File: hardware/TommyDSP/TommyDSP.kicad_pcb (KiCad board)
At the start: 2 copper layers, 35 parts, among them SW201 SW_Push, SW202 SW_Push, U201 W25Q128JVS, U202 DNF, U203 RP2350_60QFN, Y1 ABM8-272-T3

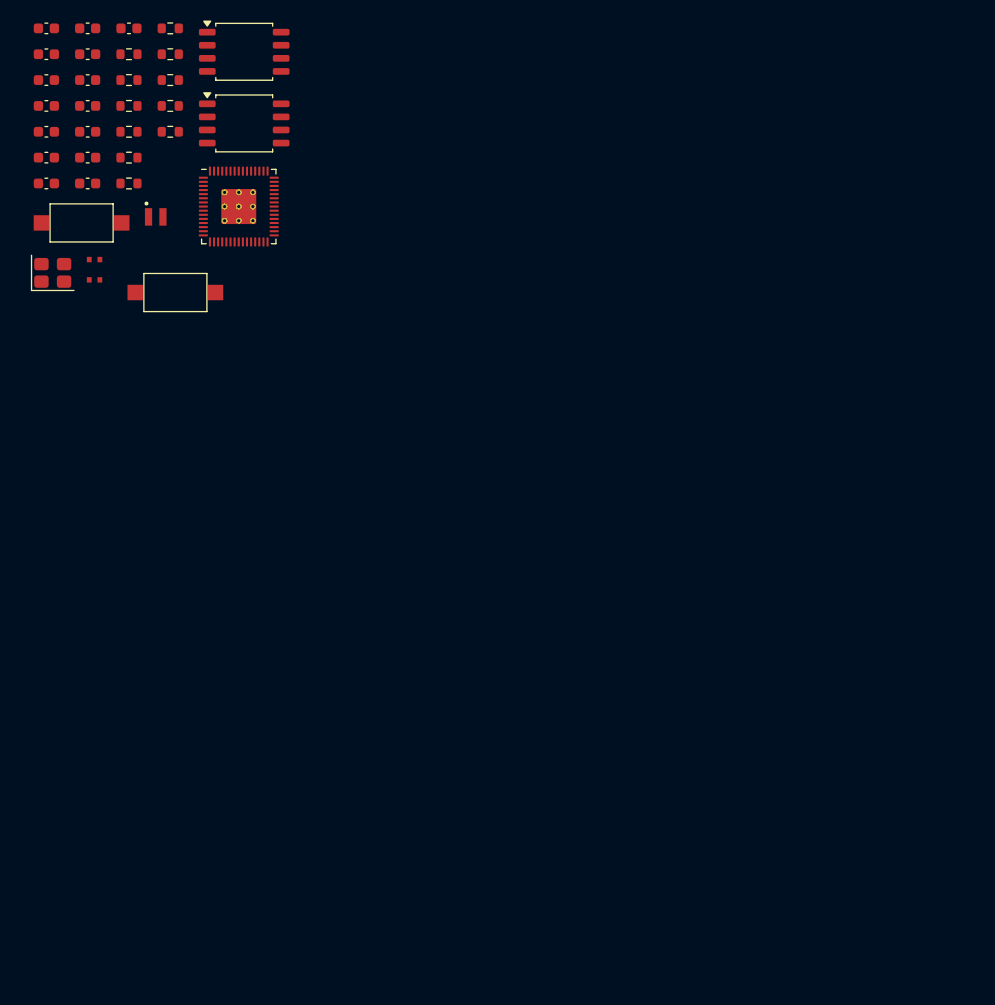
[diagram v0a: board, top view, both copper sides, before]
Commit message: hardware: finished PCB routing
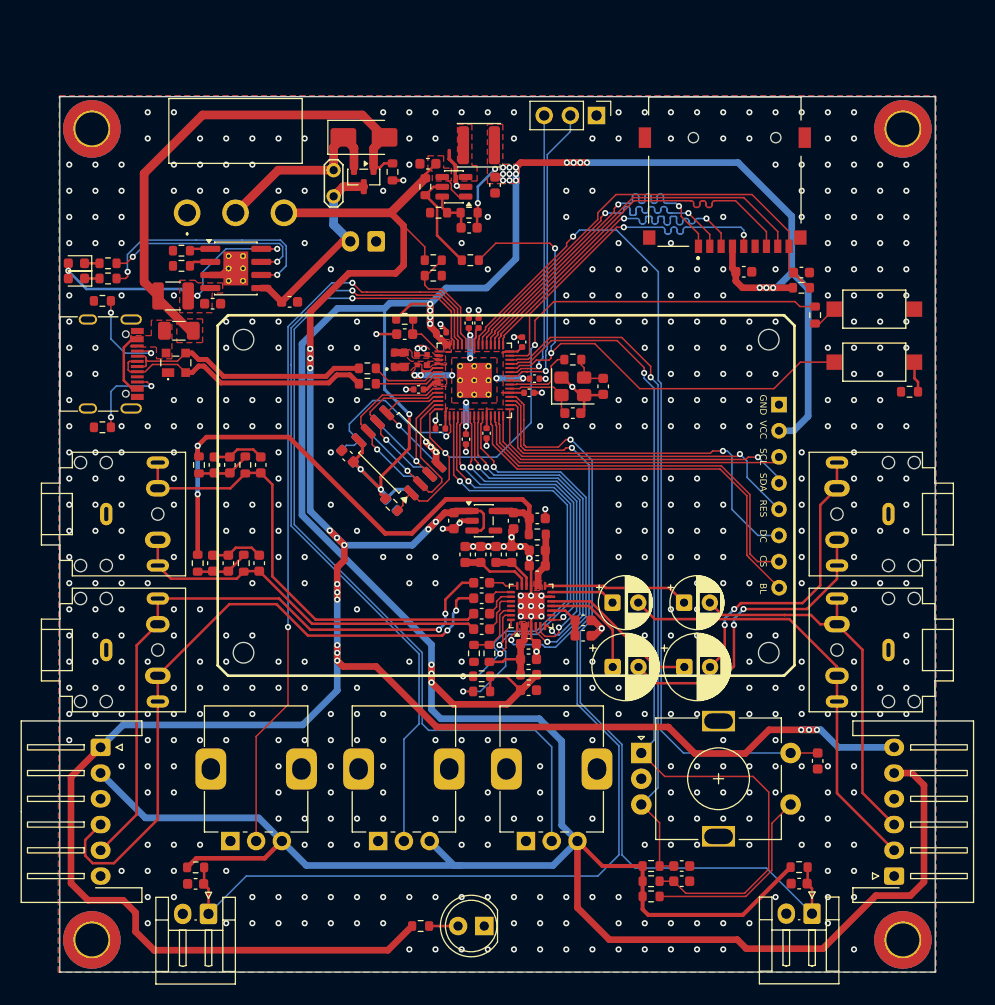
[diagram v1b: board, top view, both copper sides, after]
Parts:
- removed C3, C4: 15p, Capacitor_SMD:C_0603_1608Metric
- removed R2: 1k, Resistor_SMD:R_0603_1608Metric
- removed R209, R210: 27, Resistor_SMD:R_0603_1608Metric
- removed Y1: ABM8-272-T3, Crystal:Crystal_SMD_3225-4Pin_3.2x2.5mm
- added C216: 100n, Capacitor_SMD:C_0402_1005Metric, F.Cu at (158.1, 100.6)
- added C217: 100n, Capacitor_SMD:C_0402_1005Metric, F.Cu at (156.0, 96.8)
- added C301: 4.7u, Capacitor_SMD:C_0603_1608Metric, F.Cu at (171.9, 119.2)
- added C302: 4.7u, Capacitor_SMD:C_0603_1608Metric, F.Cu at (165.0, 112.8)
- added C303: 4.7u, Capacitor_SMD:C_0603_1608Metric, F.Cu at (162.0, 112.8)
- added C304: 100n, Capacitor_SMD:C_0603_1608Metric, F.Cu at (167.5, 109.3)
- added C305: 100n, Capacitor_SMD:C_0603_1608Metric, F.Cu at (171.9, 120.7)
- added C306: 100n, Capacitor_SMD:C_0603_1608Metric, F.Cu at (163.5, 112.8)
- added C307: 100n, Capacitor_SMD:C_0603_1608Metric, F.Cu at (160.5, 112.8)
- added C308: 4.7uF, Capacitor_SMD:C_0603_1608Metric, F.Cu at (166.7, 123.0)
- added C309: 4.7uF, Capacitor_SMD:C_0603_1608Metric, F.Cu at (167.5, 112.4)
- added C310: 100n, Capacitor_SMD:C_0603_1608Metric, F.Cu at (166.7, 121.5)
- added C311: 100n, Capacitor_SMD:C_0603_1608Metric, F.Cu at (167.5, 113.9)
- added C312: 100n, Capacitor_SMD:C_0603_1608Metric, F.Cu at (162.1, 120.1)
- added C313: 100n, Capacitor_SMD:C_0603_1608Metric, F.Cu at (162.1, 118.6)
- added C314: 1u, Capacitor_SMD:C_0603_1608Metric, F.Cu at (162.1, 117.1)
- added C315: 1u, Capacitor_SMD:C_0603_1608Metric, F.Cu at (162.1, 115.6)
- added C316: 220u, Capacitor_THT:CP_Radial_D6.3mm_P2.50mm, F.Cu at (181.8, 123.8)
- added C317: 220u, Capacitor_THT:CP_Radial_D6.3mm_P2.50mm, F.Cu at (174.8, 123.8)
- added C318: 4.7u, Capacitor_THT:CP_Radial_D5.0mm_P2.50mm, F.Cu at (181.8, 117.5)
- added C319: 4.7u, Capacitor_THT:CP_Radial_D5.0mm_P2.50mm, F.Cu at (174.8, 117.5)
- added C320: 10u, Capacitor_SMD:C_0603_1608Metric, F.Cu at (136.0, 113.7)
- added C321: 100n, Capacitor_SMD:C_0603_1608Metric, F.Cu at (137.5, 113.7)
- added C322: 10n, Capacitor_SMD:C_0603_1608Metric, F.Cu at (140.5, 113.7)
- added C323: 10u, Capacitor_SMD:C_0603_1608Metric, F.Cu at (136.2, 104.1)
- added C324: 100n, Capacitor_SMD:C_0603_1608Metric, F.Cu at (137.7, 104.1)
- added C325: 10n, Capacitor_SMD:C_0603_1608Metric, F.Cu at (140.7, 104.1)
- added C401: 4.7u, Capacitor_SMD:C_0603_1608Metric, F.Cu at (156.9, 74.9)
- added C402: 1u, Capacitor_SMD:C_0603_1608Metric, F.Cu at (159.4, 109.5)
- added C403: 10u, Capacitor_SMD:C_0603_1608Metric, F.Cu at (136.0, 88.5)
- added C404: 4.7u, Capacitor_SMD:C_0603_1608Metric, F.Cu at (165.2, 109.5)
- added C405: 120p, Capacitor_SMD:C_0603_1608Metric, F.Cu at (160.9, 81.1)
- added C406: 22u, Capacitor_SMD:C_0603_1608Metric, F.Cu at (163.4, 77.0)
- added C407: 10u, Capacitor_SMD:C_0603_1608Metric, F.Cu at (143.4, 88.3)
- added C501: 100n, Capacitor_SMD:C_0603_1608Metric, F.Cu at (134.3, 144.8)
- added C502: 100n, Capacitor_SMD:C_0603_1608Metric, F.Cu at (192.9, 144.8)
- added C503: 100n, Capacitor_SMD:C_0603_1608Metric, F.Cu at (187.6, 85.4)
- added C504: 100n, Capacitor_SMD:C_0603_1608Metric, F.Cu at (181.5, 144.6)
- added C505: 100n, Capacitor_SMD:C_0603_1608Metric, F.Cu at (181.5, 143.1)
- added C506: 100n, Capacitor_SMD:C_0603_1608Metric, F.Cu at (166.7, 126.0)
- added C507: 100n, Capacitor_SMD:C_0603_1608Metric, F.Cu at (193.2, 85.5)
- added C508: 100n, Capacitor_SMD:C_0603_1608Metric, F.Cu at (194.7, 132.9)
- added D401: LED GREEN, LED_SMD:LED_0603_1608Metric, F.Cu at (122.8, 86.0)
- added D402: LED RED, LED_SMD:LED_0603_1608Metric, F.Cu at (122.8, 84.5)
- added D403: SS34, Diode_SMD:D_SMA, F.Cu at (150.7, 72.3)
- added D404: PWR LED, LED_THT:LED_D5.0mm, F.Cu at (162.3, 148.9)
- added D501: CD143A-SR05, CD143A-SR05:CD143ASR05, F.Cu at (132.4, 94.2)
- added F501: 6V 1.1A, Fuse:Fuse_1206_3216Metric, F.Cu at (132.7, 91.1)
- added FB301: 120Ω@100MHz 2A 50mΩ@DC, Inductor_SMD:L_0603_1608Metric, F.Cu at (166.7, 124.5)
- added H101: M3 MountingHole, MountingHole:MountingHole_3.2mm_M3_DIN965_Pad_TopBottom, F.Cu at (124.2, 71.5)
- added H102: M3 MountingHole, MountingHole:MountingHole_3.2mm_M3_DIN965_Pad_TopBottom, F.Cu at (124.2, 150.2)
- added H103: M3 MountingHole, MountingHole:MountingHole_3.2mm_M3_DIN965_Pad_TopBottom, F.Cu at (203.0, 71.5)
- added H104: M3 MountingHole, MountingHole:MountingHole_3.2mm_M3_DIN965_Pad_TopBottom, F.Cu at (203.0, 150.2)
- added J401: Conn_01x02_Pin, Connector_JST:JST_XH_B2B-XH-A_1x02_P2.50mm_Vertical, B.Cu at (151.8, 82.4)
- added J501: USB_C_Receptacle_USB2.0_16P, Connector_USB:USB_C_Receptacle_G-Switch_GT-USB-7010ASV, F.Cu at (124.9, 94.3)
- added J502: PJ-307, Project:Jack_3.5mm_CUI_SJ1-3525N_Horizontal, F.Cu at (125.7, 108.9)
- added J503: XH-2.50mm Horizontal, Connector_JST:JST_EH_S2B-EH_1x02_P2.50mm_Horizontal, F.Cu at (135.6, 147.7)
- added J504: PJ-307, Project:Jack_3.5mm_CUI_SJ1-3525N_Horizontal, F.Cu at (125.7, 122.1)
- added J505: Conn_01x06_Pin, Connector_JST:JST_XH_S6B-XH-A-1_1x06_P2.50mm_Horizontal, F.Cu at (125.1, 131.6)
- added J506: PJ-307, Project:Jack_3.5mm_CUI_SJ1-3525N_Horizontal, F.Cu at (201.6, 108.9)
- added J507: XH-2.50mm Horizontal, Connector_JST:JST_EH_S2B-EH_1x02_P2.50mm_Horizontal, F.Cu at (194.2, 147.7)
- added J508: Conn_01x06_Pin, Connector_JST:JST_XH_S6B-XH-A-1_1x06_P2.50mm_Horizontal, F.Cu at (202.2, 144.1)
- added J509: Conn_01x03_Pin, Connector_PinHeader_2.54mm:PinHeader_1x03_P2.54mm_Vertical, F.Cu at (173.2, 70.2)
- added J510: PJ-307, Project:Jack_3.5mm_CUI_SJ1-3525N_Horizontal, F.Cu at (201.6, 122.1)
- added J511: Micro_SD_Card_Det1, TF-01A:TF01A, F.Cu at (185.7, 75.7)
- added JP401: Jumper_2_Open, TestPoint:TestPoint_2Pads_Pitch2.54mm_Drill0.8mm, F.Cu at (147.7, 78.0)
- added L401: 1u, Inductor_SMD:L_APV_ANR4020, F.Cu at (161.8, 73.1)
- added LCD501: 1.8'_ST7735_128x160_TFT_Module, ST7735-128x160-TFT-Module:1.8'_ST7735_128x160_TFT_Module, F.Cu at (167.8, 107.0)
- added Q401: AO3401A, Package_TO_SOT_SMD:SOT-23, F.Cu at (150.7, 76.2)
- added R101: 0, Resistor_SMD:R_0603_1608Metric, F.Cu at (161.0, 84.2)
- added R102: 4.7k, Resistor_SMD:R_0603_1608Metric, F.Cu at (162.1, 126.1)
- added R103: 4.7k, Resistor_SMD:R_0603_1608Metric, F.Cu at (162.1, 124.7)
- added R301: 0, Resistor_SMD:R_0603_1608Metric, F.Cu at (162.8, 122.4)
- added R302: 0, Resistor_SMD:R_0603_1608Metric, F.Cu at (161.3, 122.4)
- added R303: 10, Resistor_SMD:R_0603_1608Metric, F.Cu at (167.5, 110.9)
- added R304: 1k, Resistor_SMD:R_0603_1608Metric, F.Cu at (134.5, 113.7)
- added R305: 2.2k, Resistor_SMD:R_0603_1608Metric, F.Cu at (139.0, 113.7)
- added R306: 1k, Resistor_SMD:R_0603_1608Metric, F.Cu at (134.7, 104.1)
- added R307: 2.2k, Resistor_SMD:R_0603_1608Metric, F.Cu at (139.2, 104.1)
- added R401: 1k, Resistor_SMD:R_0603_1608Metric, F.Cu at (125.8, 86.0)
- added R402: 1k, Resistor_SMD:R_0603_1608Metric, F.Cu at (125.8, 84.5)
- added R403: 500k, Resistor_SMD:R_0603_1608Metric, F.Cu at (156.6, 77.1)
- added R404: 0.5, Resistor_SMD:R_1210_3225Metric, F.Cu at (132.1, 87.7)
- added R405: 225k, Resistor_SMD:R_0603_1608Metric, F.Cu at (160.9, 79.6)
- added R406: 50k, Resistor_SMD:R_0603_1608Metric, F.Cu at (157.9, 79.6)
- added R407: 1.2k, Resistor_SMD:R_0603_1608Metric, F.Cu at (132.9, 84.8)
- added R408: 0, Resistor_SMD:R_0603_1608Metric, F.Cu at (132.9, 83.3)
- added R409: 10k, Resistor_SMD:R_0603_1608Metric, F.Cu at (153.4, 75.7)
- added R410: 1k, Resistor_SMD:R_0603_1608Metric, F.Cu at (156.2, 148.9)
- added R501: 100k, Resistor_SMD:R_0603_1608Metric, F.Cu at (157.4, 84.2)
- added R502: 100k, Resistor_SMD:R_0603_1608Metric, F.Cu at (157.4, 85.8)
- added R503: 5.1k, Resistor_SMD:R_0603_1608Metric, F.Cu at (125.3, 88.2)
- added R504: 5.1k, Resistor_SMD:R_0603_1608Metric, F.Cu at (125.3, 100.5)
- added R505: 100k, Resistor_SMD:R_0603_1608Metric, F.Cu at (134.3, 143.2)
- added R506: 100k, Resistor_SMD:R_0603_1608Metric, F.Cu at (192.9, 143.2)
- added R507: 100k, Resistor_SMD:R_0603_1608Metric, F.Cu at (178.6, 144.6)
- added R508: 100k, Resistor_SMD:R_0603_1608Metric, F.Cu at (178.6, 143.1)
- added R509: 100k, Resistor_SMD:R_0603_1608Metric, F.Cu at (193.2, 86.9)
- added R510: 100k, Resistor_SMD:R_0603_1608Metric, F.Cu at (178.6, 146.0)
- added RV501: ALPS RK09L, Potentiometer_THT:Potentiometer_Alps_RK09K_Single_Vertical, F.Cu at (137.7, 140.7)
- added RV502: ALPS RK09L, Potentiometer_THT:Potentiometer_Alps_RK09K_Single_Vertical, F.Cu at (152.1, 140.7)
- added RV503: ALPS RK09L, Potentiometer_THT:Potentiometer_Alps_RK09K_Single_Vertical, F.Cu at (166.4, 140.7)
- added S401: SS-12D06L5, SS-12D06L5:SS12D06L5, F.Cu at (133.5, 79.7)
- added SW501: RotaryEncoder_Switch_MP, Rotary_Encoder:RotaryEncoder_Alps_EC11E-Switch_Vertical_H20mm, F.Cu at (177.6, 132.1)
- added U301: ES8388, Package_DFN_QFN:QFN-28-1EP_4x4mm_P0.45mm_EP2.6x2.6mm, F.Cu at (166.9, 117.8)
- added U401: TPS7A2033PDBVR, Package_TO_SOT_SMD:SOT-23-5, F.Cu at (162.3, 109.5)
- added U402: TPS62A01APDDC, Package_TO_SOT_SMD:SOT-23-6, F.Cu at (159.4, 77.1)
- added U403: TP4056-42-ESOP8, Package_SO:SOIC-8-1EP_3.9x4.9mm_P1.27mm_EP2.41x3.3mm_ThermalVias, F.Cu at (138.2, 85.0)
- added Y201: ABM8-272-T3, Crystal:Crystal_SMD_3225-4Pin_3.2x2.5mm, F.Cu at (170.9, 96.5)
- C202, U202: moved to B.Cu
- C205: value 100n -> 15p
- C206: value 4.7u -> 15p
- C207: value 4.7u -> 100n; footprint Capacitor_SMD:C_0603_1608Metric -> Capacitor_SMD:C_0402_1005Metric
- C208: value 100n -> 4.7u
- C209: value 100n -> 4.7u; footprint Capacitor_SMD:C_0603_1608Metric -> Capacitor_SMD:C_0402_1005Metric
- C210, C211, C212, C213, C214, C215: footprint Capacitor_SMD:C_0603_1608Metric -> Capacitor_SMD:C_0402_1005Metric
- R202: value 0 -> DNF; moved to B.Cu
- R203: value 0 -> 1k
- R204: value DNF -> 33
- R205: value DNF -> 1k
- R207: value 33 -> 27
- R208: value 1k -> 27
- moved R203 79.9 mm to (203.6, 97.0), turned to 180 degrees
- moved SW202 78.2 mm to (200.2, 94.2), turned to 180 degrees
- moved SW201 67.9 mm to (200.2, 89.0), turned to 180 degrees
- moved R205 67.8 mm to (194.5, 89.6), turned to -90 degrees
- moved C206 58.5 mm to (173.9, 96.5), turned to -90 degrees
- moved C205 58.0 mm to (170.9, 99.1)
- moved C209 53.6 mm to (167.2, 95.8)
- moved C202 51.2 mm to (153.3, 108.0), turned to -45 degrees
- moved C210 50.6 mm to (160.6, 101.6), turned to -90 degrees
- moved R206 50.6 mm to (170.9, 93.9)
- moved C212 48.5 mm to (162.6, 101.0), turned to -90 degrees
- moved R201 48.5 mm to (153.3, 108.0), turned to -45 degrees
- moved C214 47.4 mm to (166.7, 97.1)
- moved C201 46.8 mm to (149.1, 103.3), turned to 135 degrees
- moved C213 45.8 mm to (166.0, 92.2), turned to 90 degrees
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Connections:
- net /MCU-Core/RUN renamed /RUN
- C205 pad 1: +1V1 -> /MCU-Core/XIN
- C206 pad 1: /MCU-Core/VREG_AVDD -> Net-(C206-Pad1)
- C208 pad 1: +1V1 -> /MCU-Core/VREG_AVDD
- C209 pad 1: +3V3 -> +1V1
- C210 pad 1: +3V3 -> +1V1
- R201 pad 1: /MCU-Core/GPIO0 -> +3V3
- R201 pad 2: /MCU-Core/FLASH_SS -> /MCU-Core/QSPI_SS
- R202 pad 1: /MCU-Core/QSPI_SS -> +3V3
- R202 pad 2: /MCU-Core/FLASH_SS -> /MCU-Core/GPIO0
- R203 pad 1: /MCU-Core/GPIO0 -> Net-(R203-Pad1)
- R203 pad 2: /MCU-Core/FLASH2_SS -> GND
- R204 pad 2: /MCU-Core/FLASH_SS -> /MCU-Core/VREG_AVDD
- R205 pad 1: +3V3 -> /MCU-Core/QSPI_SS
- R205 pad 2: /MCU-Core/FLASH2_SS -> /MCU-Core/~{USB_BOOT}
- R206 pad 1: Net-(R206-Pad1) -> /MCU-Core/XOUT
- R206 pad 2: GND -> Net-(C206-Pad1)
- R207 pad 1: +3V3 -> /USB_D+
- R207 pad 2: /MCU-Core/VREG_AVDD -> Net-(U203-USB_DP)
- R208 pad 1: /MCU-Core/QSPI_SS -> /USB_D-
- R208 pad 2: /MCU-Core/~{USB_BOOT} -> Net-(U203-USB_DM)
- SW202 pad 1: Net-(R206-Pad1) -> Net-(R203-Pad1)
- U201 pad 1: /MCU-Core/FLASH_SS -> /MCU-Core/QSPI_SS
- U202 pad 1: /MCU-Core/FLASH2_SS -> /MCU-Core/GPIO0
- U203 pad 10: /MCU-Core/GPIO7 -> /CODEC_I2S_MCLK
- U203 pad 12: /MCU-Core/GPIO8 -> /LCD_BL
- U203 pad 13: /MCU-Core/GPIO9 -> /LCD_SPI_CS
- U203 pad 14: /MCU-Core/GPIO10 -> /LCD_SPI_SCK
- U203 pad 15: /MCU-Core/GPIO11 -> /LCD_SPI_MOSI
- U203 pad 16: /MCU-Core/GPIO12 -> /LCD_RST
- U203 pad 17: /MCU-Core/GPIO13 -> /LCD_DC
- U203 pad 18: /MCU-Core/GPIO14 -> /PEDAL_1
- U203 pad 19: /MCU-Core/GPIO15 -> /PEDAL_2
- U203 pad 24: /MCU-Core/SWCLK -> /SWCLK
- U203 pad 25: /MCU-Core/SWD -> /SWD
- U203 pad 27: /MCU-Core/GPIO16 -> /ROTARY_ENCODER_CLK
- U203 pad 28: /MCU-Core/GPIO17 -> /ROTARY_ENCODER_DT
- U203 pad 29: /MCU-Core/GPIO18 -> /SD_CLK/SCK
- U203 pad 3: /MCU-Core/GPIO1 -> /CODEC_I2C_SCL
- U203 pad 31: /MCU-Core/GPIO19 -> /SD_CMD/MOSI
- U203 pad 32: /MCU-Core/GPIO20 -> /SD_DAT0/MISO
- U203 pad 33: /MCU-Core/GPIO21 -> /SD_DAT1
- U203 pad 34: /MCU-Core/GPIO22 -> /SD_DAT2
- U203 pad 35: /MCU-Core/GPIO23 -> /SD_DAT3/CS
- U203 pad 36: /MCU-Core/GPIO24 -> /SD_DET
- U203 pad 37: /MCU-Core/GPIO25 -> /ROTARY_ENCODER_BUTTON
- U203 pad 4: /MCU-Core/GPIO2 -> /CODEC_I2C_SDA
- U203 pad 40: /MCU-Core/GPIO26_ADC0 -> /VBAT_ADC
- U203 pad 41: /MCU-Core/GPIO27_ADC1 -> /R_POT_1
- U203 pad 42: /MCU-Core/GPIO28_ADC2 -> /R_POT_2
- U203 pad 43: /MCU-Core/GPIO29_ADC3 -> /R_POT_3
- U203 pad 5: /MCU-Core/GPIO3 -> /CODEC_I2S_DOUT
- U203 pad 7: /MCU-Core/GPIO4 -> /CODEC_I2S_DIN
- U203 pad 8: /MCU-Core/GPIO5 -> /CODEC_I2S_LRCK
- U203 pad 9: /MCU-Core/GPIO6 -> /CODEC_I2S_SCLK
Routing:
- net +3V3: track 0.00 -> 401.0 mm, vias 0 -> 28
- net VCC: track 0.00 -> 243.6 mm, vias 0 -> 17
- net /PEDAL_1: track 0.00 -> 99.7 mm, vias 0 -> 1
- net /ROTARY_ENCODER_CLK: track 0.00 -> 86.9 mm, vias 0 -> 1
- net /R_POT_3: track 0.00 -> 86.5 mm, vias 0 -> 1
- net /ROTARY_ENCODER_BUTTON: track 0.00 -> 85.3 mm, vias 0 -> 1
- net /PEDAL_2: track 0.00 -> 79.5 mm, vias 0 -> 1
- net /R_POT_2: track 0.00 -> 77.3 mm, vias 0 -> 1
- net /R_POT_1: track 0.00 -> 74.2 mm, vias 0 -> 2
- net /ROTARY_ENCODER_DT: track 0.00 -> 67.3 mm, vias 0 -> 1
- net GND: track 0.00 -> 65.2 mm, vias 0 -> 532
- net /LINEIN_L: track 0.00 -> 64.2 mm, vias 0 -> 2
- net /MCU-Core/QSPI_SS: track 0.00 -> 63.5 mm, vias 0 -> 2
- net /LINEIN_R: track 0.00 -> 61.9 mm, vias 0 -> 2
- net +3.3VA: track 0.00 -> 56.1 mm, vias 0 -> 2
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- added copper zone on F.Cu, net +1V1
- added copper zone on B.Cu, net +3V3
- added copper zone on F.Cu, net +3V3
- added copper zone on F.Cu, net /Audio/AVDD
- added copper zone on F.Cu, net /Audio/DVDD
- added copper zone on F.Cu, net /MCU-Core/VREG_LX
- added copper zone on B.Cu, net GND
- added copper zone on F.Cu, net GND
- added copper zone on F.Cu, net Net-(D401-A)
- added copper zone on F.Cu, net Net-(D501-REF)
- added copper zone on F.Cu, net Net-(U402-SW)
- added copper zone on F.Cu, net VBUS
- added copper zone on F.Cu, net VCC
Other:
- board outline added: 85 x 85 mm
- board text added: "LCD POSITION: X:167.8 mm Y:106.975 mm"

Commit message: hardware: finalize PCB design
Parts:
- added C509: 100n, Capacitor_SMD:C_0603_1608Metric, F.Cu at (148.1, 146.0)
- added G501: qwiic_Logo, SparkFun-Qwiic:qwiic_5.5mm, F.Cu at (156.1, 152.2)
- added J512: Qwiic, Connector_JST:JST_SH_SM04B-SRSS-TB_1x04-1MP_P1.00mm_Horizontal, F.Cu at (149.3, 150.1)
- added REF**: ESD-Logo_6.6x6mm_SilkScreen, Symbol:ESD-Logo_6.6x6mm_SilkScreen, F.Cu at (199.9, 79.7)
- added REF**: KiCad-Logo2_6mm_SilkScreen, Symbol:KiCad-Logo2_6mm_SilkScreen, B.Cu at (178.7, 106.5)
- J502, J504, J506, J510: value PJ-307 -> AudioJack3_SwitchTR
- J505: value Conn_01x06_Pin -> EXT.IN
- J508: value Conn_01x06_Pin -> EXT.OUT
- moved R203 1.19 mm to (204.4, 97.9), turned to -90 degrees
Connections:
- U203 pad 3: /CODEC_I2C_SCL -> /I2C_SCL
- U203 pad 4: /CODEC_I2C_SDA -> /I2C_SDA
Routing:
- net /CODEC_I2C_SCL: track 46.6 -> 80.7 mm, vias 3 -> 5
- net /CODEC_I2C_SDA: track 48.0 -> 81.1 mm, vias 3 -> 5
- net GND: track 65.2 -> 97.3 mm, vias 532 -> 792
- net +3V3: track 401.0 -> 426.6 mm, vias 28 -> 29
- net /ROTARY_ENCODER_CLK: track 86.9 -> 87.5 mm
- net /ROTARY_ENCODER_DT: track 67.3 -> 68.0 mm
- net VCC: track 243.6 -> 243.2 mm, vias 17 -> 19
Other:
- board text added: "3V3"
- board text added: "BAT+ BAT-"
- board text added: "BOOT0"
- board text added: "CHRG FULL"
- board text added: "CLK"
- board text added: "DEBUG"
- board text added: "DIO"
- board text added: "ECE5 Group 6 Jason Mua'az Smrethi"
- board text added: "EXT.IN"
- board text added: "EXT.OUT"
- board text added: "GND"
- board text added: "GND SIG"
- board text added: "HEADPHONE"
- board text added: "Jason Chen 2026.02"
- board text added: "KNOB1"
- board text added: "KNOB2"
- board text added: "KNOB3"
- board text added: "LIN"
- board text added: "LINE IN"
- board text added: "LINE OUT"
- board text added: "LOUT"
- board text added: "MIC"
- board text added: "ON"
- board text added: "PWR"
- board text added: "Put it back!"
- board text added: "RESET"
- board text added: "RIN"
- board text added: "ROTARY ENCODER"
- board text added: "ROUT"
- board text added: "SW1"
- board text added: "SW2"
- board text added: "TF CARD"
- board text added: "TommyDSP REV 1.0.0"
- board text added: "VCC"

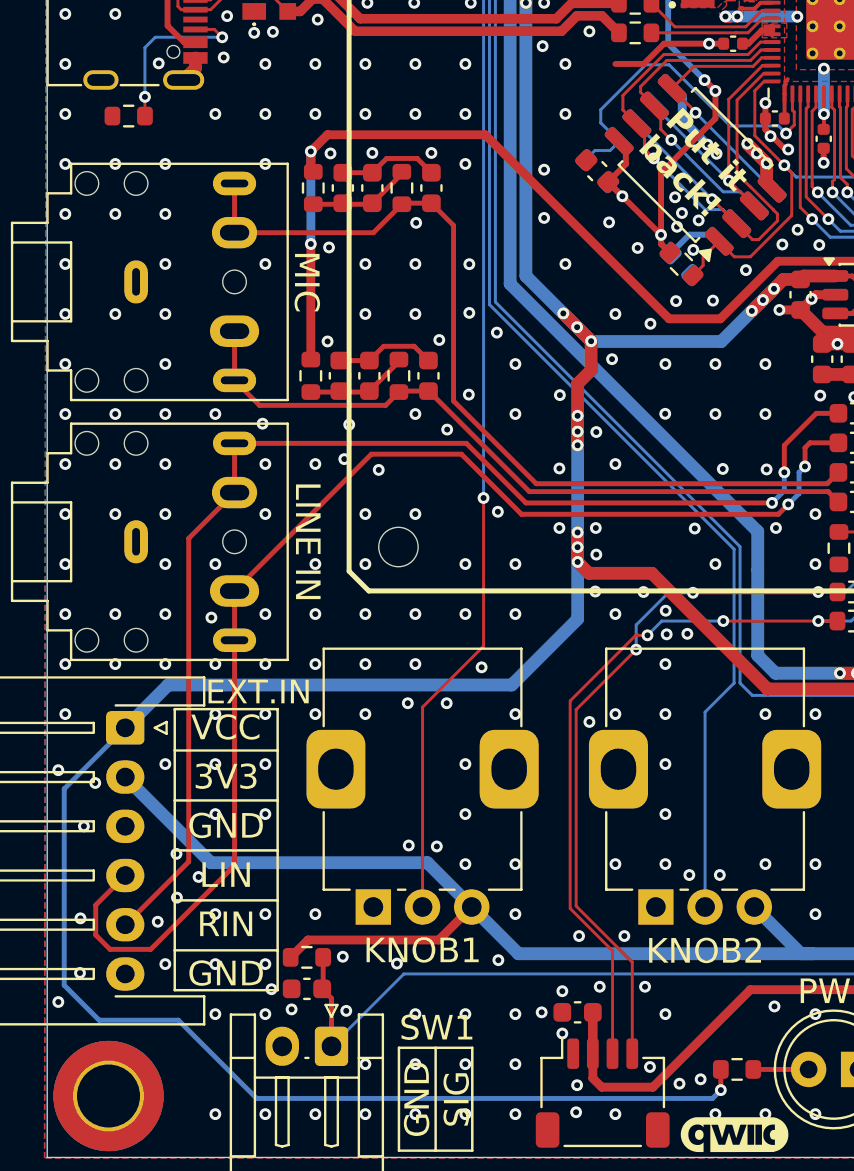
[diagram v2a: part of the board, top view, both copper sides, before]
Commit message: hardware: minor silkscreen text adjustments
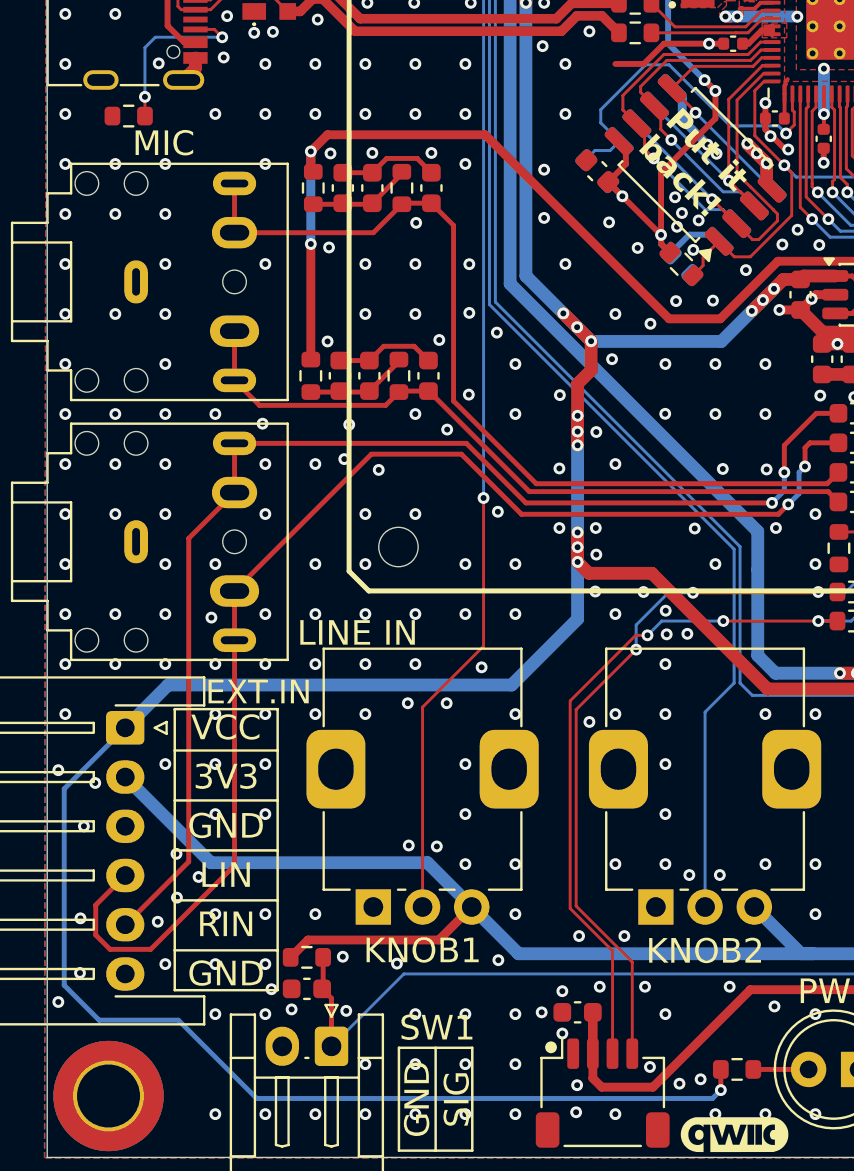
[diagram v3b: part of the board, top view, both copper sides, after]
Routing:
- net GND: vias 792 -> 793
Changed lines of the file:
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@@
 		)
 	)
+	(gr_circle
+		(center 146.725 147.775)
+		(end 146.975 147.775)
+		(stroke
+			(width 0.1)
+			(type default)
+		)
+		(fill yes)
+		(layer "F.SilkS")
+	)
 	(gr_line
 		(start 127.6125 142.85)
@@
 	)
 	(gr_text "MIC"
-		(at 134.3 108.9 270)
+		(at 127.05 101.875 0)
 		(layer "F.SilkS")
 		(effects
@@
 	)
 	(gr_text "LINE IN"
-		(at 134.35 122.1 270)
+		(at 136.9 126.75 0)
 		(layer "F.SilkS")
 		(effects
@@
 	)
 	(gr_text "LCD POSITION:\nX:167.8 mm\nY:106.975 mm"
-		(at 212.175 125.25 0)
+		(at 177.575 173.425 0)
 		(layer "Dwgs.User")
 		(effects
@@
 		(size 0.6)
 		(drill 0.3)
+		(layers "F.Cu" "B.Cu")
+		(free yes)
+		(net 2)
+	)
+	(via
+		(at 155.8 144.7)
+		(size 0.6)
+		(drill 0.3)

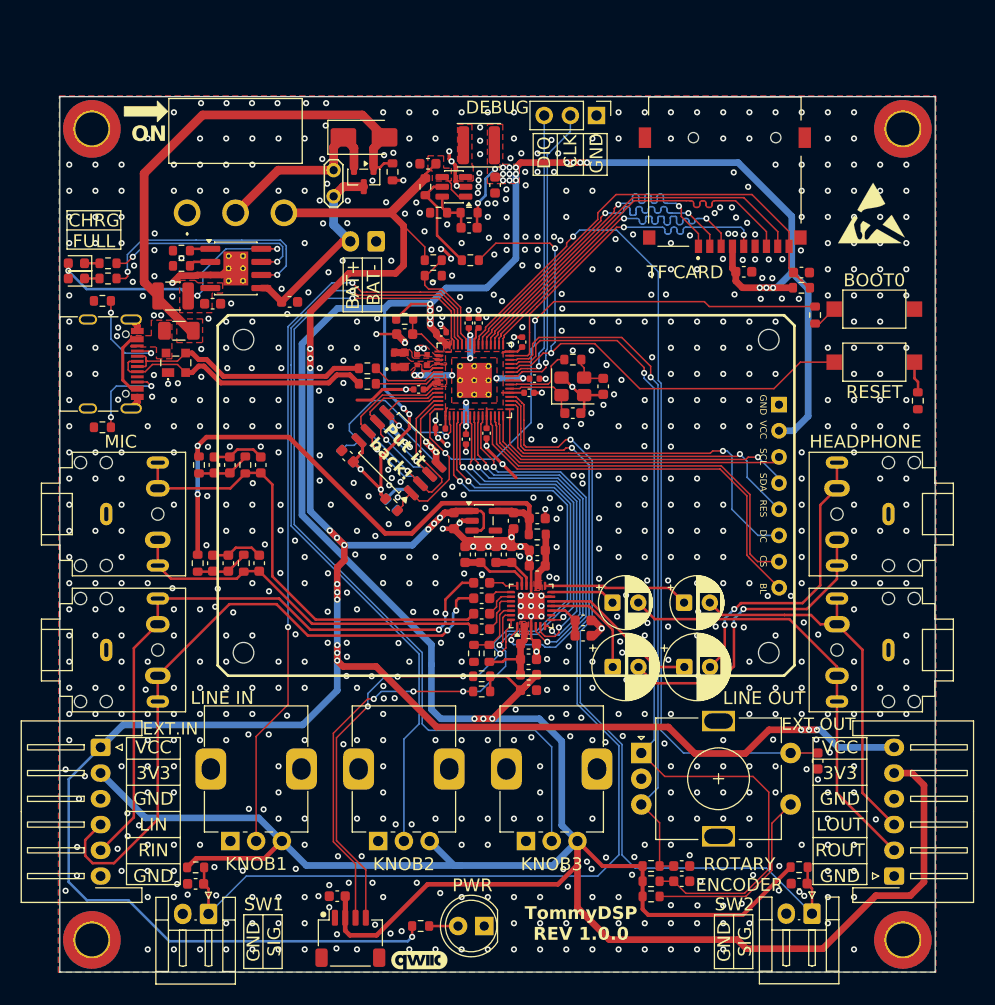
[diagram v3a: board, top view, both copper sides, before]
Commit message: hardware: fix incorrect audio jack symbol
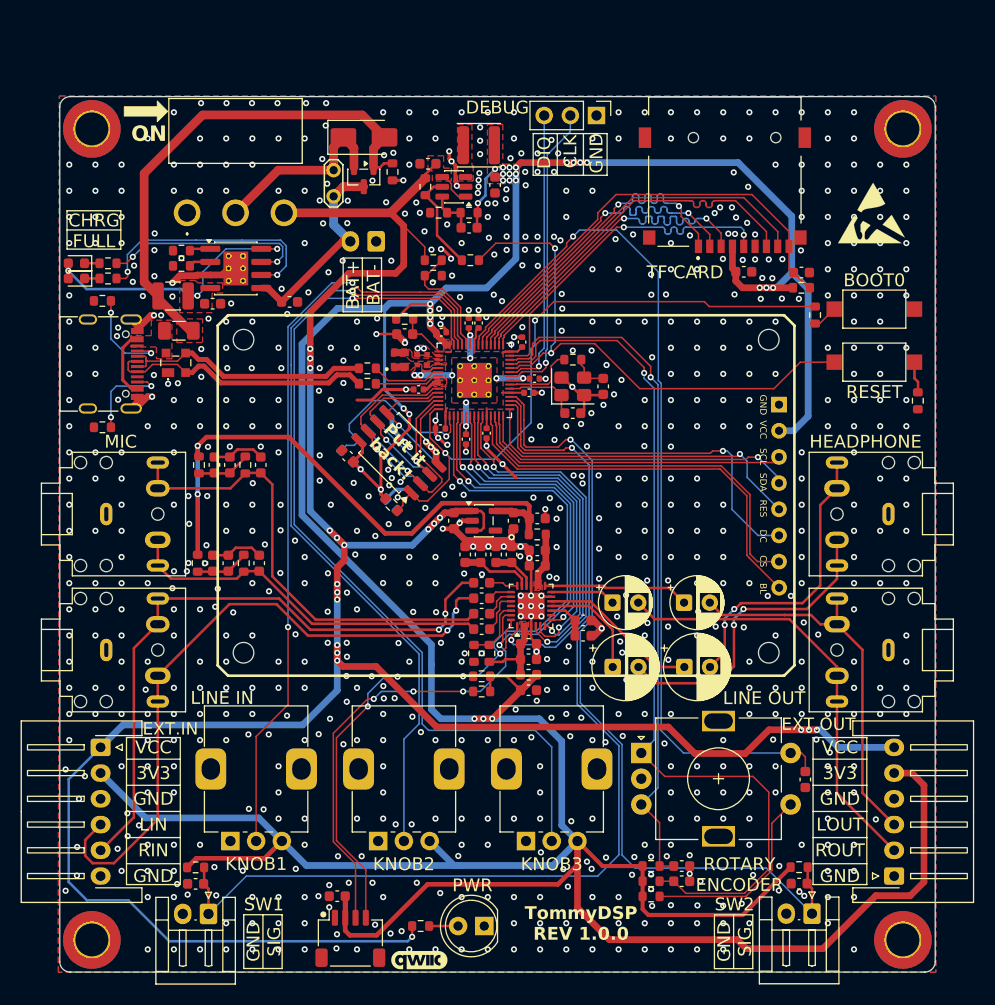
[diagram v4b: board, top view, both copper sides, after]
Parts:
- moved C508 2.16 mm to (193.5, 134.7)
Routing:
- net GND: track 97.3 -> 102.2 mm, vias 793 -> 815
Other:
- outline, holes or cut-outs redrawn
